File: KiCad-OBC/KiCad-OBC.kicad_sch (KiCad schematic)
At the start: 3 parts

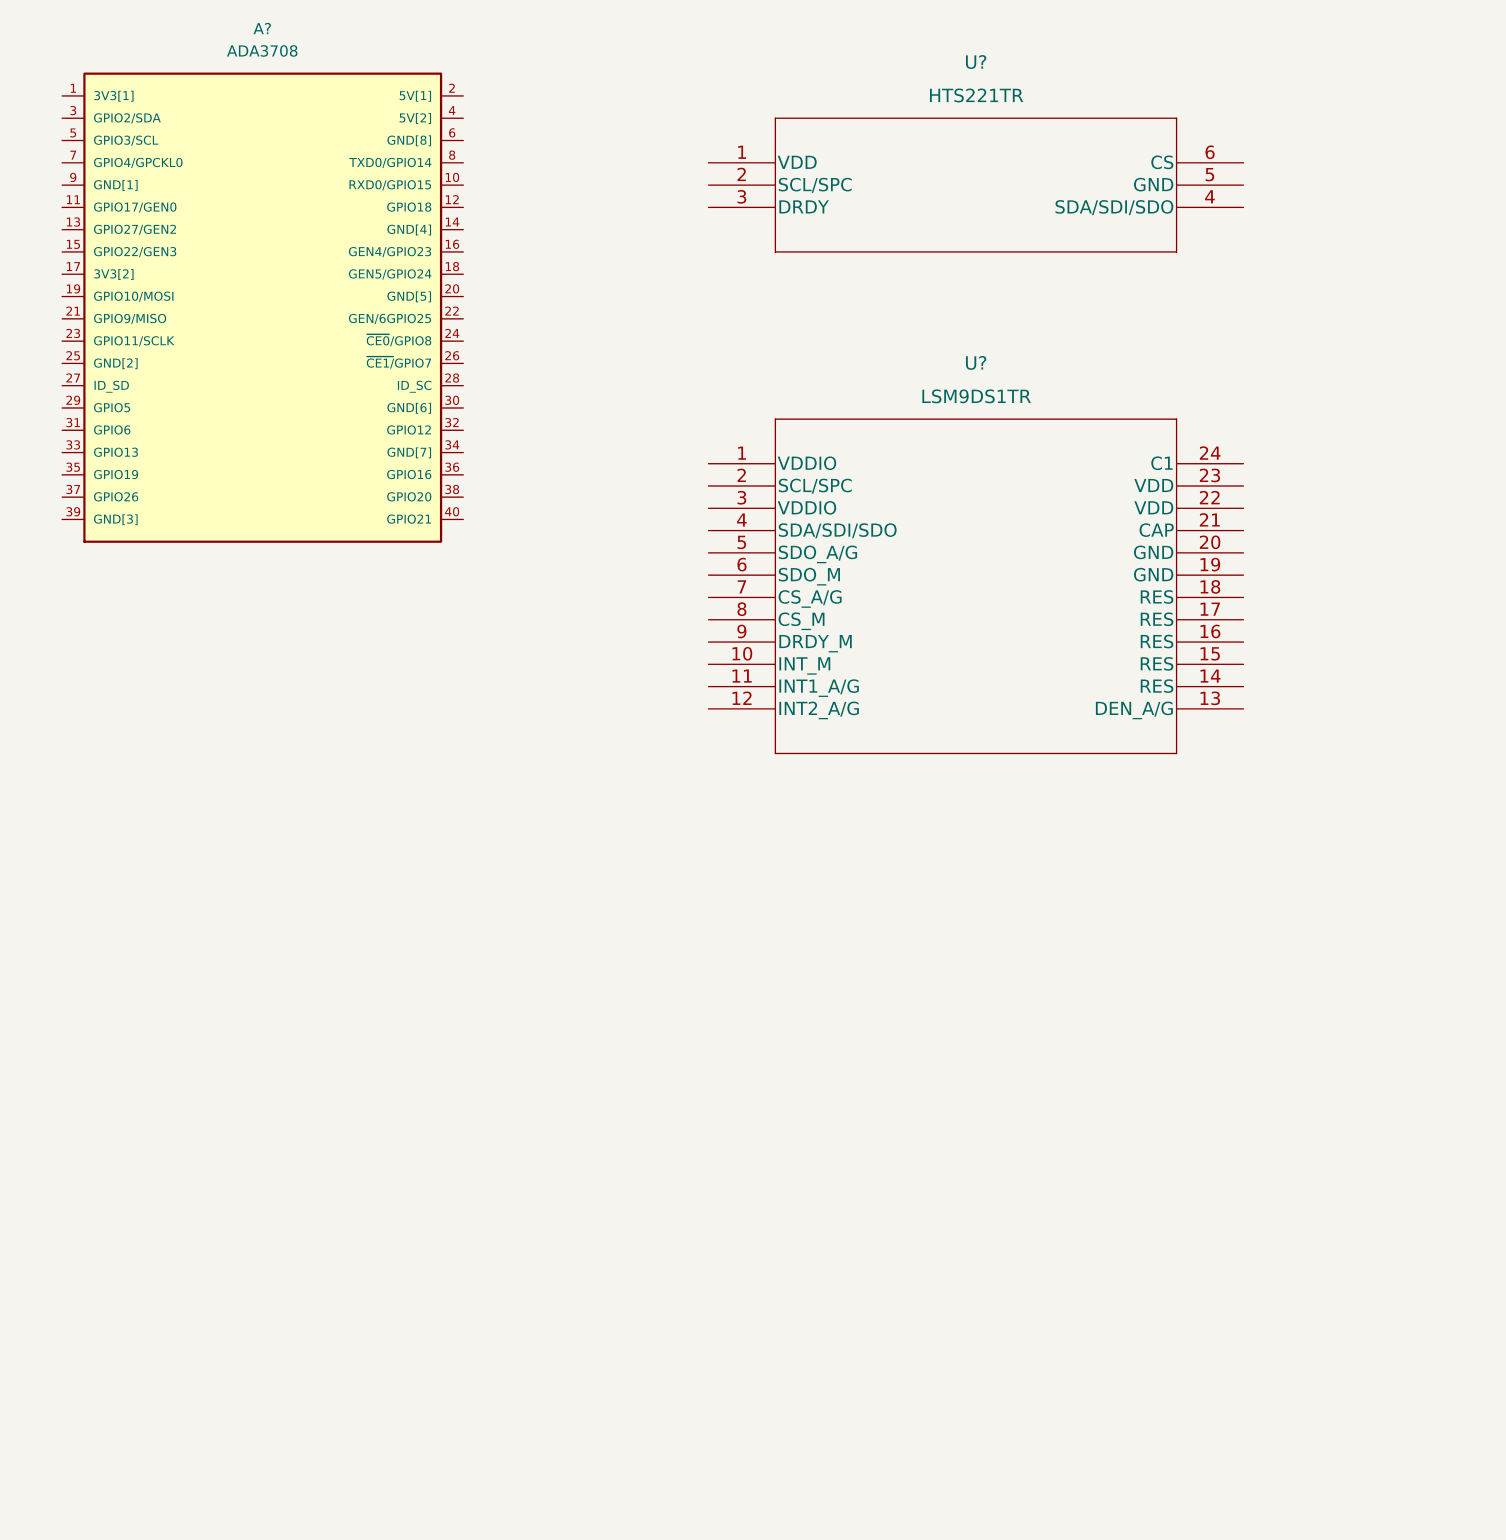
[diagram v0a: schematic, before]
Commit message: updated foot prints of the sensors
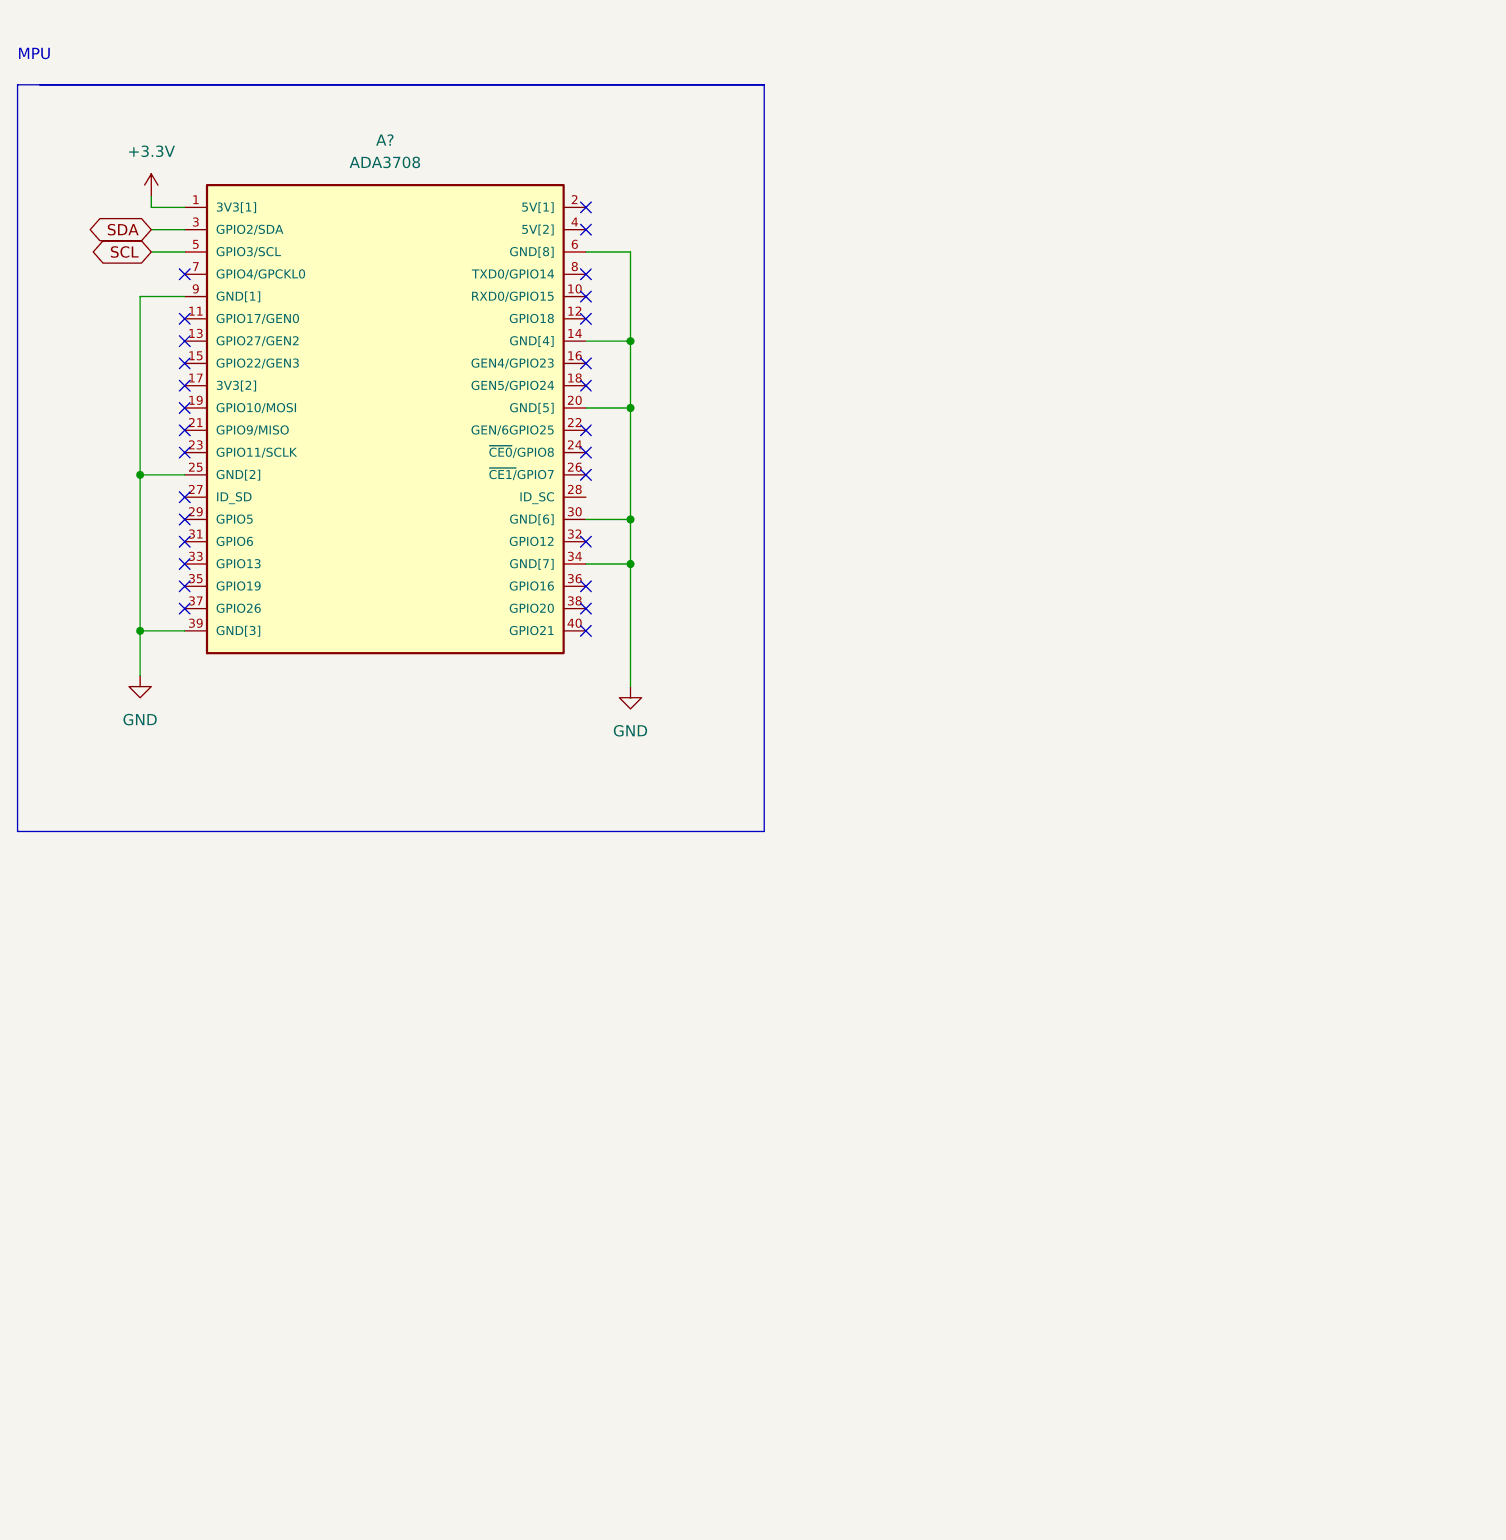
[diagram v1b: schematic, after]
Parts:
- removed U?: LSM9DS1TR, LGA-24_3X3P5X1_STM, symbol OBC:LSM9DS1TR
- removed U?: HTS221TR, HLGA-6L_2X2_STM, symbol OBC:HTS221TR
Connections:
- net +3V3: now reaches A?.1 (3V3[1])
- net GND: now reaches A?.14 (GND[4])
- net GND: now also A?.20 (GND[5]), A?.25 (GND[2]), A?.30 (GND[6]), A?.34 (GND[7]), A?.39 (GND[3]), A?.6 (GND[8]), A?.9 (GND[1])
- net SDA: now reaches A?.3 (GPIO2/SDA)
- net SCL: now reaches A?.5 (GPIO3/SCL)
- no-connect marks 0 -> 28
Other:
- note added: "MPU"
- company: (none) -> UniSat
- title: (none) -> UNEPG-2022-Module 04 - OBC
- moved on the sheet: A?

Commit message: schematics finished
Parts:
- added C? (x5): 100n, symbol Device:C_Small
- added C? (x2): 10n, symbol Device:C_Small
- added R?: 10K, symbol Device:R_Small
- added U?: HTS221, XDCR_HTS221, symbol OBC:HTS221
- added U?: LSM9DS1, PQFN24P43_350X300X102L35X23N, symbol OBC:LSM9DS1
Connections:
- net +3V3: now also C?.1, C?.1, C?.1, C?.1, C?.1, R?.1, U?.1 (VDD), U?.1 (VDDIO), U?.22 (VDD), U?.23 (VDD), U?.3 (VDDIO), U?.6 (CS), U?.7 (CS_A/G), U?.8 (CS_M)
- net GND: now also C?.1, C?.1, C?.2, C?.2, C?.2, C?.2, C?.2, U?.14 (RES), U?.15 (RES), U?.16 (RES), U?.17 (RES), U?.18 (RES), U?.19 (GND), U?.20 (GND), U?.5 (GND), U?.5 (SDO_A/G), U?.6 (SDO_M)
- net SCL: now also U?.2 (SCL/SPC), U?.2 (SCL/SPC)
- net SDA: now also U?.4 (SDA/SDI/SDO), U?.4 (SDA/SDI/SDO)
- new net: C?.2, U?.24 (C1)
- new net: R?.2, U?.13 (DEN_A/G)
- new net: C?.2, U?.21 (CAP)
- no-connect marks 28 -> 33
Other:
- note added: "Accelerometer, Gyroscope , Magnitometer"
- note added: "Humidity, Temperature"

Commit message: start obc again with new place
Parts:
- removed C? (x5): 100n, symbol Device:C_Small
- removed C? (x2): 10n, symbol Device:C_Small
- removed R?: 10K, symbol Device:R_Small
- removed U?: HTS221, XDCR_HTS221, symbol OBC:HTS221
- removed U?: LSM9DS1, PQFN24P43_350X300X102L35X23N, symbol OBC:LSM9DS1
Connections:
- no-connect marks 33 -> 28
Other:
- note removed: "Accelerometer, Gyroscope , Magnitometer"
- note removed: "Humidity, Temperature"

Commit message: schematics done, foot prints assigned
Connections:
- no-connect marks 28 -> 30
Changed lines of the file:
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@@
   (junction (at 88.9 76.2) (diameter 0) (color 0 0 0 0)
   )
+  (no_connect (at 83.82 68.58))
+  (no_connect (at 88.9 91.44))
   (no_connect (at 83.82 73.66))
   (no_connect (at 38.1 68.58))
